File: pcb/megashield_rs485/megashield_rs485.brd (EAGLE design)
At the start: 101.6 x 53.3 mm, 21 parts, among them J11 DYNAMIXEL_RS485, U1 RS485

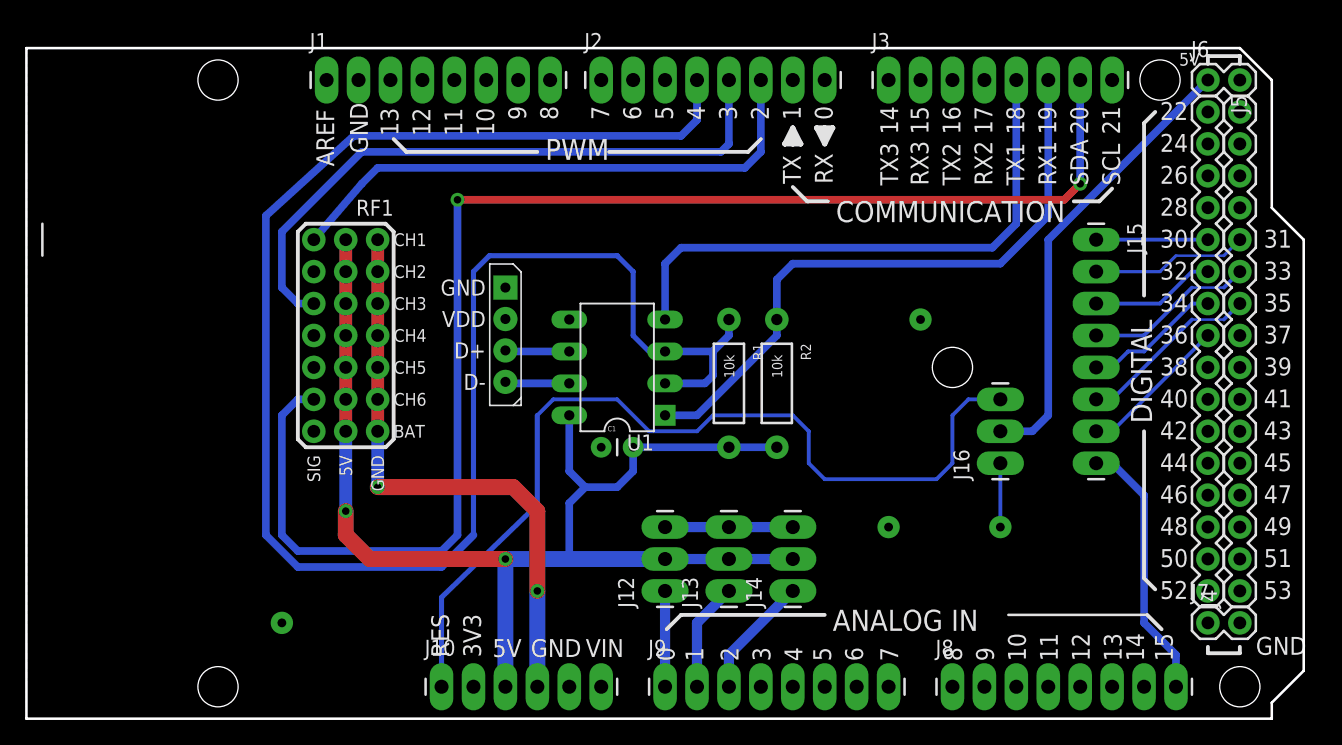
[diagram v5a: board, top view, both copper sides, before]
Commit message: Fix PCB dimension for better fit on Arduino board
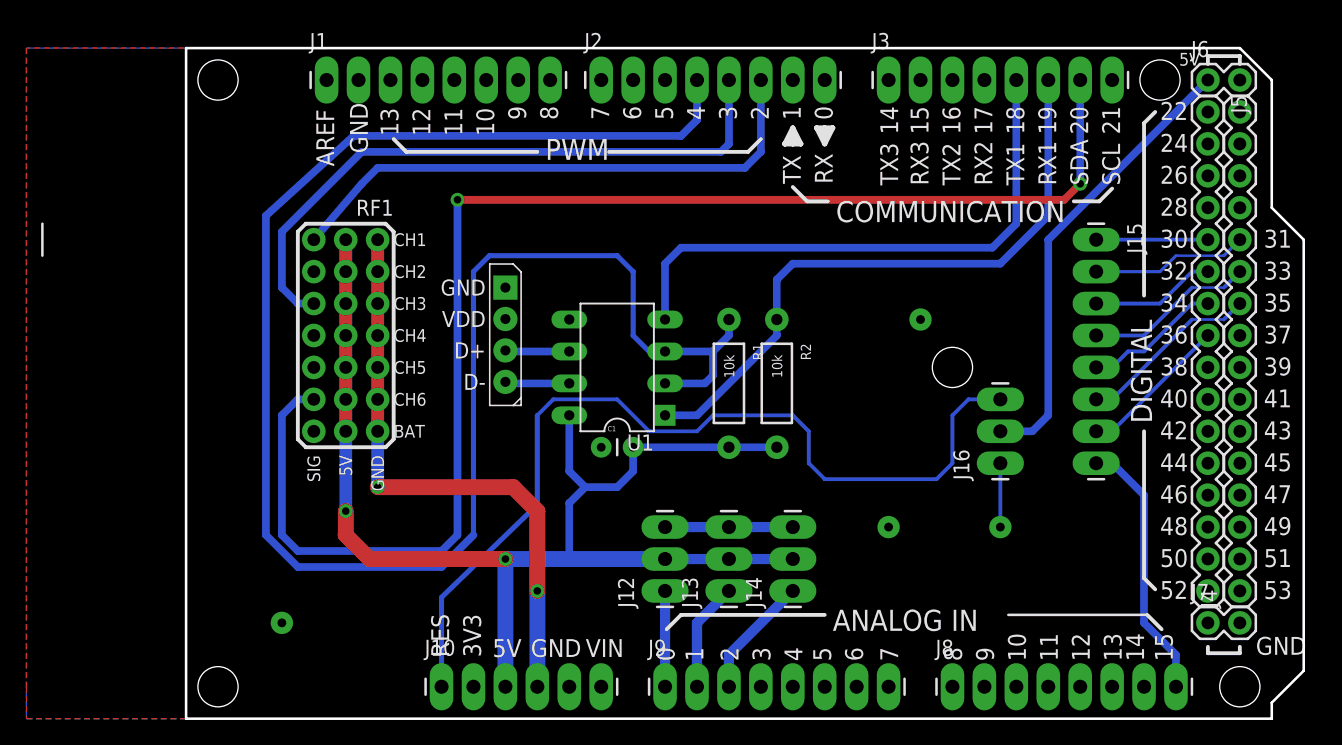
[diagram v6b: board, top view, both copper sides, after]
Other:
- board size 101.6 x 53.3 mm -> 88.9 x 53.3 mm
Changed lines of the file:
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@@
 <wire x1="0" y1="53.34" x2="0" y2="0" width="0.254" layer="51"/>
 <wire x1="1.27" y1="39.37" x2="1.27" y2="36.83" width="0.2032" layer="21"/>
-<wire x1="0" y1="0" x2="99.06" y2="0" width="0.2032" layer="20"/>
+<wire x1="12.7" y1="0" x2="99.06" y2="0" width="0.2032" layer="20"/>
 <wire x1="99.06" y1="0" x2="99.06" y2="1.27" width="0.2032" layer="20"/>
 <wire x1="99.06" y1="1.27" x2="101.6" y2="3.81" width="0.2032" layer="20"/>
@@
 <wire x1="99.06" y1="40.64" x2="99.06" y2="50.8" width="0.2032" layer="20"/>
 <wire x1="99.06" y1="50.8" x2="96.52" y2="53.34" width="0.2032" layer="20"/>
-<wire x1="96.52" y1="53.34" x2="0" y2="53.34" width="0.2032" layer="20"/>
-<wire x1="0" y1="53.34" x2="0" y2="0" width="0.2032" layer="20"/>
+<wire x1="96.52" y1="53.34" x2="12.7" y2="53.34" width="0.2032" layer="20"/>
+<wire x1="12.7" y1="53.34" x2="12.7" y2="0" width="0.2032" layer="20"/>
 <text x="64.135" y="6.985" size="1.6764" layer="21" font="vector" ratio="15">ANALOG IN</text>
 <text x="24.4812" y="43.9288" size="1.4224" layer="21" font="vector" ratio="15" rot="R90">AREF</text>

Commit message: PCB with LCD
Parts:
- removed J15: (no value), mecatronica_eagle_lib:1X08_LONGPADS
- removed J16: (no value), mecatronica_eagle_lib:1X03_LONGPADS
- added LCD: LCD_SHIELD, mecatronica_eagle_lib:LCD_SHIELD
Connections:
- net 5V@1: now also LCD.5V; no longer J16.2
- net A15: now also LCD.BS; no longer J15.8
- net D30: now also LCD.D4; no longer J15.1
- net D31: now also LCD.D5; no longer J15.2
- net D32: now also LCD.D6; no longer J15.3
- net D33: now also LCD.D7; no longer J15.4
- net D34: now also LCD.RS; no longer J15.5
- net D35: now also LCD.EN; no longer J15.6
- net D36: now also LCD.BLC; no longer J15.7
- net GND: now also LCD.GND@1, LCD.GND@2, LCD.GND@3; no longer J16.1
- net RES: no longer J16.3
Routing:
- net D30: track 8.89 -> 0.00 mm
- net D32: track 9.94 -> 4.86 mm
- net GND: track 47.1 -> 42.1 mm, vias 6 -> 5
- net D31: track 12.5 -> 7.40 mm
- net D33: track 13.5 -> 9.72 mm
- net 5V@1: track 36.3 -> 33.7 mm
- net RES: track 72.2 -> 69.7 mm
- net D36: track 12.0 -> 10.8 mm
- net D35: track 14.6 -> 13.3 mm
- net D34: track 11.0 -> 9.72 mm
- net A15: track 21.2 -> 19.9 mm
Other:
- board size 88.9 x 53.3 mm -> 133.4 x 53.3 mm
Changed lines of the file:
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@@
 <?xml version="1.0" encoding="utf-8"?>
 <!DOCTYPE eagle SYSTEM "eagle.dtd">
-<eagle version="7.4.0">
+<eagle version="7.6.0">
 <drawing>
 <settings>
@@
 <layer number="50" name="dxf" color="7" fill="1" visible="no" active="yes"/>
 <layer number="51" name="tDocu" color="6" fill="1" visible="yes" active="yes"/>
-<layer number="52" name="bDocu" color="7" fill="1" visible="yes" active="yes"/>
+<layer number="52" name="bDocu" color="7" fill="1" visible="no" active="yes"/>
 <layer number="53" name="tGND_GNDA" color="7" fill="9" visible="no" active="no"/>
 <layer number="54" name="bGND_GNDA" color="1" fill="9" visible="no" active="no"/>
@@
 <layer number="230" name="230bmp" color="7" fill="1" visible="no" active="yes"/>
 <layer number="231" name="231bmp" color="7" fill="1" visible="no" active="yes"/>
+<layer number="232" name="Eagle3D_PG2" color="7" fill="1" visible="no" active="no"/>
+<layer number="233" name="Eagle3D_PG3" color="7" fill="1" visible="no" active="no"/>
 <layer number="248" name="Housing" color="7" fill="1" visible="no" active="yes"/>
 <layer number="249" name="Edge" color="7" fill="1" visible="no" active="yes"/>
@@
 <wire x1="0" y1="53.34" x2="0" y2="0" width="0.254" layer="51"/>
 <wire x1="1.27" y1="39.37" x2="1.27" y2="36.83" width="0.2032" layer="21"/>
-<wire x1="12.7" y1="0" x2="99.06" y2="0" width="0.2032" layer="20"/>
-<wire x1="99.06" y1="0" x2="99.06" y2="1.27" width="0.2032" layer="20"/>
-<wire x1="99.06" y1="1.27" x2="101.6" y2="3.81" width="0.2032" layer="20"/>
-<wire x1="101.6" y1="3.81" x2="101.6" y2="38.1" width="0.2032" layer="20"/>
-<wire x1="101.6" y1="38.1" x2="99.06" y2="40.64" width="0.2032" layer="20"/>
-<wire x1="99.06" y1="40.64" x2="99.06" y2="50.8" width="0.2032" layer="20"/>
-<wire x1="99.06" y1="50.8" x2="96.52" y2="53.34" width="0.2032" layer="20"/>
-<wire x1="96.52" y1="53.34" x2="12.7" y2="53.34" width="0.2032" layer="20"/>
+<wire x1="12.7" y1="0" x2="143.51" y2="0" width="0.2032" layer="20"/>
+<wire x1="143.51" y1="53.34" x2="12.7" y2="53.34" width="0.2032" layer="20"/>
 <wire x1="12.7" y1="53.34" x2="12.7" y2="0" width="0.2032" layer="20"/>
 <text x="64.135" y="6.985" size="1.6764" layer="21" font="vector" ratio="15">ANALOG IN</text>
@@
 <rectangle x1="0" y1="30.48" x2="11.43" y2="53.34" layer="42"/>
 <rectangle x1="0" y1="0" x2="15.24" y2="13.97" layer="42"/>
+<wire x1="143.51" y1="53.34" x2="146.05" y2="50.8" width="0.254" layer="20"/>
+<wire x1="146.05" y1="50.8" x2="146.05" y2="2.54" width="0.254" layer="20"/>
+<wire x1="146.05" y1="2.54" x2="143.51" y2="0" width="0.254" layer="20"/>
 </plain>
 <attributes>
@@
 <element name="R1" library="mecatronica_eagle_lib" package="AXIAL-0.4" value="10k" x="55.88" y="26.67" rot="R270"/>
 <element name="R2" library="mecatronica_eagle_lib" package="AXIAL-0.4" value="10k" x="59.69" y="26.67" rot="R270"/>
-<element name="J15" library="mecatronica_eagle_lib" package="1X08_LONGPADS" value="" x="85.09" y="38.1" rot="R270"/>
-<element name="J16" library="mecatronica_eagle_lib" package="1X03_LONGPADS" value="" x="77.47" y="20.32" rot="R90"/>
+<element name="LCD" library="mecatronica_eagle_lib" package="LCD_SHIELD" value="LCD_SHIELD" x="-11.43" y="-59.69"/>
 </elements>
 <signals>
 <signal name="RES">
 <contactref element="J10" pad="1"/>
-<contactref element="J16" pad="3"/>
 <wire x1="33.02" y1="2.54" x2="33.02" y2="9.652" width="0.4064" layer="16"/>
 <wire x1="33.02" y1="9.652" x2="40.64" y2="17.018" width="0.4064" layer="16"/>
@@
 <wire x1="73.66" y1="20.32" x2="73.66" y2="24.13" width="0.3048" layer="16"/>
 <wire x1="73.66" y1="24.13" x2="74.93" y2="25.4" width="0.3048" layer="16"/>
-<wire x1="74.93" y1="25.4" x2="77.47" y2="25.4" width="0.3048" layer="16"/>
 </signal>
 <signal name="5V">
@@
 <signal name="D31">
 <contactref element="J4" pad="12"/>
-<contactref element="J15" pad="2"/>
-<wire x1="85.09" y1="35.56" x2="90.17" y2="35.56" width="0.254" layer="16"/>
 <wire x1="90.17" y1="35.56" x2="91.44" y2="36.83" width="0.254" layer="16"/>
 <wire x1="91.44" y1="36.83" x2="95.25" y2="36.83" width="0.2032" layer="16"/>
 <wire x1="95.25" y1="36.83" x2="96.52" y2="38.1" width="0.254" layer="16"/>
+<contactref element="LCD" pad="D5"/>
+<wire x1="53.34" y1="-6.35" x2="90.17" y2="35.56" width="0" layer="19" extent="16-16"/>
 </signal>
 <signal name="D33">
 <contactref element="J4" pad="11"/>
-<contactref element="J15" pad="4"/>
-<wire x1="85.09" y1="30.48" x2="88.9" y2="30.48" width="0.3048" layer="16"/>
 <wire x1="88.9" y1="30.48" x2="92.71" y2="34.29" width="0.3048" layer="16"/>
 <wire x1="92.71" y1="34.29" x2="95.25" y2="34.29" width="0.2032" layer="16"/>
 <wire x1="95.25" y1="34.29" x2="96.52" y2="35.56" width="0.3048" layer="16"/>
+<contactref element="LCD" pad="D7"/>
+<wire x1="48.26" y1="-6.35" x2="88.9" y2="30.48" width="0" layer="19" extent="16-16"/>
 </signal>
 <signal name="D35">
 <contactref element="J4" pad="10"/>
-<contactref element="J15" pad="6"/>
-<wire x1="85.09" y1="25.4" x2="86.36" y2="25.4" width="0.3048" layer="16"/>
 <wire x1="86.36" y1="25.4" x2="92.71" y2="31.75" width="0.3048" layer="16"/>
 <wire x1="92.71" y1="31.75" x2="95.25" y2="31.75" width="0.2032" layer="16"/>
 <wire x1="95.25" y1="31.75" x2="96.52" y2="33.02" width="0.3048" layer="16"/>
+<contactref element="LCD" pad="EN"/>
+<wire x1="41.656" y1="-6.35" x2="86.36" y2="25.4" width="0" layer="19" extent="16-16"/>
 </signal>
 <signal name="D37">
@@
 <signal name="D30">
 <contactref element="J5" pad="5"/>
-<contactref element="J15" pad="1"/>
-<wire x1="85.09" y1="38.1" x2="93.98" y2="38.1" width="0.3048" layer="16"/>
+<contactref element="LCD" pad="D4"/>
+<wire x1="55.88" y1="-6.35" x2="93.98" y2="38.1" width="0" layer="19" extent="1-1"/>
 </signal>
 <signal name="D32">
 <contactref element="J5" pad="6"/>
-<contactref element="J15" pad="3"/>
-<wire x1="85.09" y1="33.02" x2="90.17" y2="33.02" width="0.3048" layer="16"/>
 <wire x1="90.17" y1="33.02" x2="92.71" y2="35.56" width="0.3048" layer="16"/>
 <wire x1="92.71" y1="35.56" x2="93.98" y2="35.56" width="0.3048" layer="16"/>
+<contactref element="LCD" pad="D6"/>
+<wire x1="50.8" y1="-6.35" x2="90.17" y2="33.02" width="0" layer="19" extent="16-16"/>
 </signal>
 <signal name="D34">
 <contactref element="J5" pad="7"/>
-<contactref element="J15" pad="5"/>
-<wire x1="85.09" y1="27.94" x2="86.36" y2="27.94" width="0.3048" layer="16"/>
 <wire x1="86.36" y1="27.94" x2="87.63" y2="29.21" width="0.3048" layer="16"/>
 <wire x1="87.63" y1="29.21" x2="88.9" y2="29.21" width="0.3048" layer="16"/>
 <wire x1="88.9" y1="29.21" x2="92.71" y2="33.02" width="0.3048" layer="16"/>
 <wire x1="92.71" y1="33.02" x2="93.98" y2="33.02" width="0.3048" layer="16"/>
+<contactref element="LCD" pad="RS"/>
+<wire x1="44.196" y1="-6.35" x2="86.36" y2="27.94" width="0" layer="19" extent="16-16"/>
 </signal>
 <signal name="D36">
 <contactref element="J5" pad="8"/>
-<contactref element="J15" pad="7"/>
-<wire x1="85.09" y1="22.86" x2="86.36" y2="22.86" width="0.3048" layer="16"/>
 <wire x1="86.36" y1="22.86" x2="93.98" y2="30.48" width="0.3048" layer="16"/>
+<contactref element="LCD" pad="BLC"/>
+<wire x1="39.116" y1="-6.35" x2="86.36" y2="22.86" width="0" layer="19" extent="16-16"/>
 </signal>
 <signal name="D38">
@@
 <signal name="A15">
 <contactref element="J8" pad="8"/>
-<contactref element="J15" pad="8"/>
-<wire x1="85.09" y1="20.32" x2="86.36" y2="20.32" width="0.6096" layer="16"/>
 <wire x1="86.36" y1="20.32" x2="88.9" y2="17.78" width="0.6096" layer="16"/>
 <wire x1="88.9" y1="17.78" x2="88.9" y2="7.62" width="0.6096" layer="16"/>
 <wire x1="88.9" y1="7.62" x2="91.44" y2="5.08" width="0.6096" layer="16"/>
 <wire x1="91.44" y1="5.08" x2="91.44" y2="2.54" width="0.6096" layer="16"/>
+<contactref element="LCD" pad="BS"/>
+<wire x1="53.34" y1="-54.61" x2="91.44" y2="2.54" width="0" layer="19" extent="1-1"/>
 </signal>
 <signal name="A0">
@@
 <polygon width="0.2032" layer="16" isolate="0.3048">
 <vertex x="0" y="0"/>
-<vertex x="99.06" y="0"/>
-<vertex x="99.06" y="1.27"/>
-<vertex x="101.6" y="3.81"/>
-<vertex x="101.6" y="38.1"/>
-<vertex x="99.06" y="40.64"/>
-<vertex x="99.06" y="50.8"/>
-<vertex x="96.52" y="53.34"/>
-<vertex x="21.971" y="53.34"/>
+<vertex x="143.51" y="0"/>
+<vertex x="146.05" y="2.54"/>
+<vertex x="146.05" y="50.8"/>
+<vertex x="143.51" y="53.34"/>
 <vertex x="0" y="53.34"/>
 </polygon>
@@
 <via x="20.32" y="7.62" extent="1-16" drill="0.7" diameter="1.778" shape="square"/>
 <via x="68.58" y="15.24" extent="1-16" drill="0.7" diameter="1.778" shape="square"/>
-<via x="77.47" y="15.24" extent="1-16" drill="0.7" diameter="1.778" shape="square"/>
 <via x="71.12" y="31.75" extent="1-16" drill="0.7" diameter="1.778" shape="square"/>
-<contactref element="J16" pad="1"/>
-<wire x1="77.47" y1="20.32" x2="77.47" y2="15.24" width="0.3048" layer="16"/>
+<contactref element="LCD" pad="GND@1"/>
+<contactref element="LCD" pad="GND@2"/>
+<contactref element="LCD" pad="GND@3"/>
+<wire x1="40.64" y1="2.54" x2="28.956" y2="-6.35" width="0" layer="19" extent="1-1"/>
+<wire x1="43.18" y1="-54.61" x2="28.956" y2="-6.35" width="0" layer="19" extent="1-1"/>
+<wire x1="45.72" y1="-54.61" x2="43.18" y2="-54.61" width="0" layer="19" extent="1-1"/>
 </signal>
 <signal name="N$4">
@@
 <contactref element="J6" pad="2"/>
 <contactref element="J6" pad="1"/>
-<contactref element="J16" pad="2"/>
 <wire x1="81.28" y1="38.1" x2="93.98" y2="50.8" width="0.6096" layer="16"/>
-<wire x1="77.47" y1="22.86" x2="80.01" y2="22.86" width="0.6096" layer="16"/>
 <wire x1="80.01" y1="22.86" x2="81.28" y2="24.13" width="0.6096" layer="16"/>
 <wire x1="81.28" y1="24.13" x2="81.28" y2="38.1" width="0.6096" layer="16"/>
+<contactref element="LCD" pad="5V"/>
 <wire x1="93.98" y1="50.8" x2="96.52" y2="50.8" width="0" layer="19" extent="1-1"/>
+<wire x1="40.64" y1="-54.61" x2="80.01" y2="22.86" width="0" layer="19" extent="16-16"/>
 </signal>
 </signals>

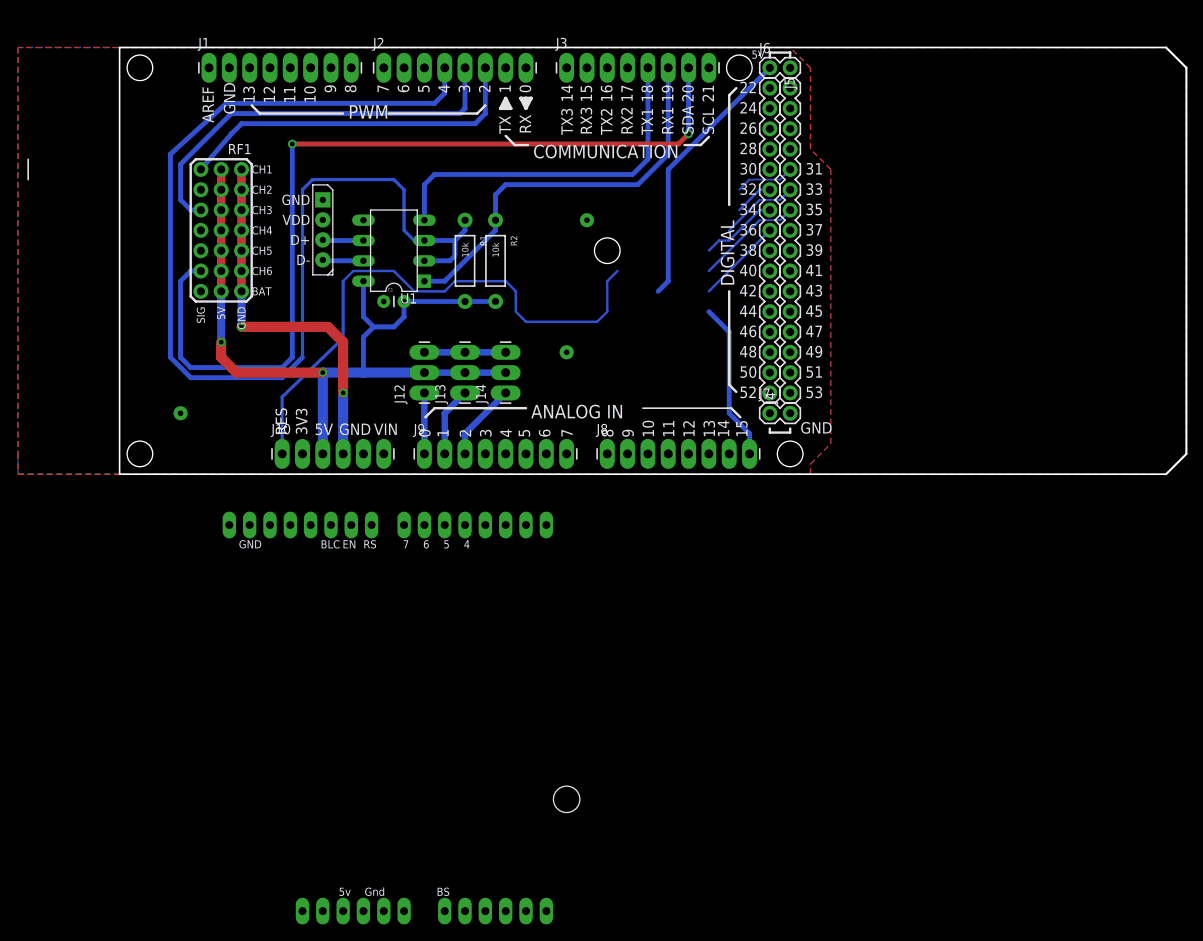
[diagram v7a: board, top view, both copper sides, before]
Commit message: Add nRF24l01
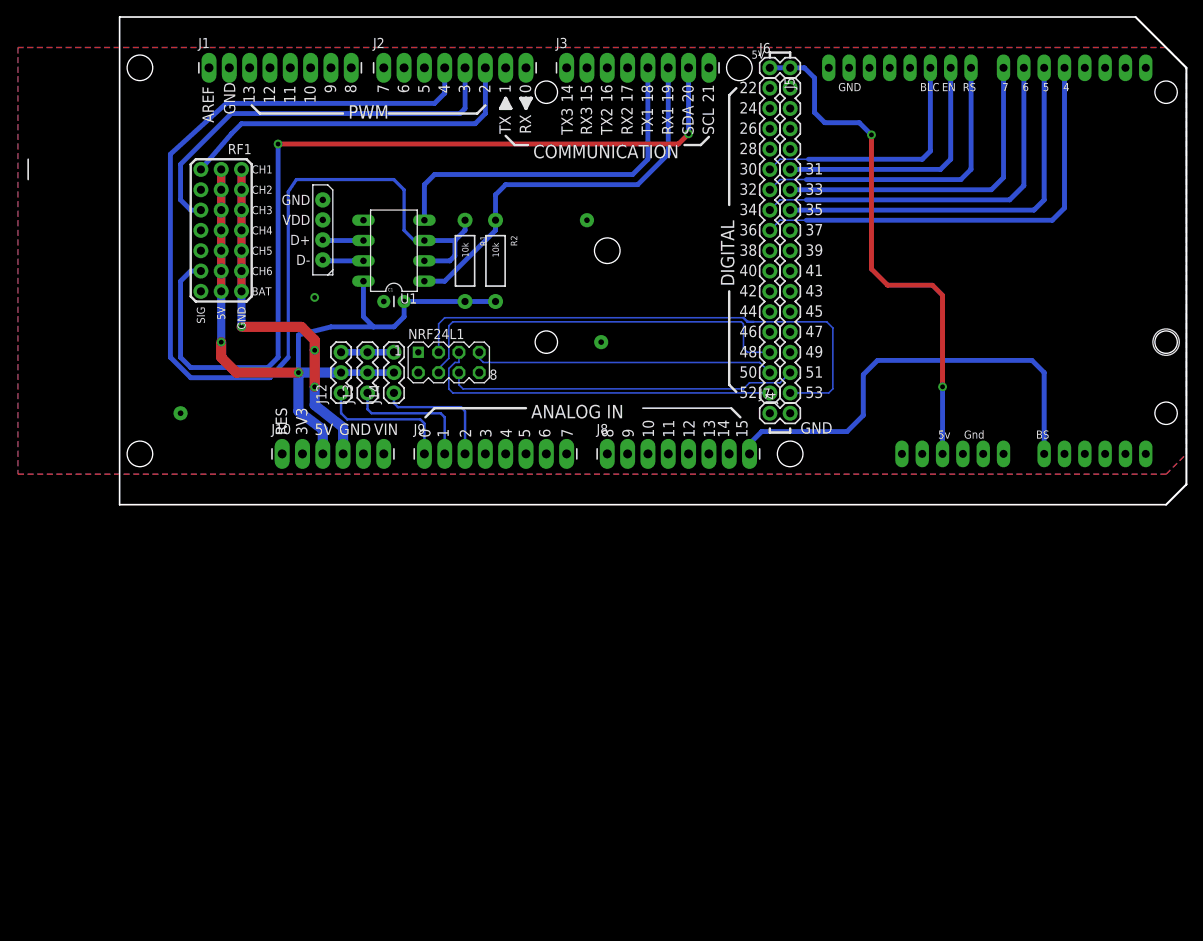
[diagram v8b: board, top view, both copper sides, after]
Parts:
- added NRF24L1: (no value), mecatronica_eagle_lib:NRF
- J12, J13, J14: device mecatronica_eagle_lib:1X03_LONGPADS -> mecatronica_eagle_lib:1X03
- moved LCD 94.2 mm to (63.5, -2.54)
- moved J14 14.0 mm to (47.0, 10.2)
- moved J13 12.2 mm to (43.7, 10.2)
- moved J12 10.4 mm to (40.4, 10.2)
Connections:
- new net N$10: NRF24L1.2
- net D30: now also LCD.BLC; no longer LCD.D4
- net D31: now also LCD.EN; no longer LCD.D5
- net D32: now also LCD.RS; no longer LCD.D6
- net D34: now also LCD.D6; no longer LCD.RS
- net D35: now also LCD.D5; no longer LCD.EN
- net D36: now also LCD.D4; no longer LCD.BLC
- net D48: now also NRF24L1.4
- net D50: now also NRF24L1.7
- net D51: now also NRF24L1.6
- net D52: now also NRF24L1.5
- net D53: now also NRF24L1.3
- net GND: now also NRF24L1.P$1
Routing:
- net RES: track 69.7 -> 0.00 mm
- net D53: track 0.00 -> 66.8 mm
- net D48: track 0.00 -> 50.1 mm
- net D52: track 0.00 -> 45.7 mm
- net D36: track 10.8 -> 55.5 mm
- net D51: track 0.00 -> 44.0 mm
- net D34: track 9.72 -> 47.7 mm
- net D50: track 0.00 -> 37.8 mm
- net A15: track 19.9 -> 56.2 mm
- net D35: track 13.3 -> 48.8 mm
- net D32: track 4.86 -> 38.9 mm
- net 5V@1: track 33.7 -> 65.5 mm, vias 0 -> 2
- net D30: track 0.00 -> 31.4 mm
- net D33: track 9.72 -> 41.0 mm
- net D31: track 7.40 -> 32.0 mm
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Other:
- board size 133.4 x 53.3 mm -> 133.4 x 61 mm
